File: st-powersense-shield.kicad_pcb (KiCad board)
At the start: 2 copper layers, 7 parts, among them P1 Left_Header, P2 IDD, P3 Right_Header, U1 MAX4378

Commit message: Generated and added manufacturing data. Also added logos to repository.
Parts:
- added G***: UoB_Logo, UoB_Logo-sm-15, F.Cu at (131.8, 108.0)
- added G***: LOGO, LOGO-mageec-smaller, F.Cu at (108.9, 103.8)
- added P4: MEAS_2, SIL-3, F.Cu at (117.9, 88.4)
- added P5: AMP_4, SIL-2, F.Cu at (134.0, 87.5)
- added P6: MEAS_4, SIL-3, F.Cu at (135.3, 93.2)
- added P7: MEAS_3, SIL-3, F.Cu at (135.3, 101.5)
- P1: value Left_Header -> Left_Discovery_Header
- P3: value Right_Header -> Right_Discovery_Header
- moved C2 43.4 mm to (125.7, 85.9), turned to 180 degrees
- moved C1 36.7 mm to (125.9, 89.0), turned to 180 degrees
- moved U1 30.5 mm to (126.2, 96.7), turned to 270 degrees
- moved R1 23.4 mm to (115.8, 99.5), turned to 270 degrees
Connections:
- P1 pad 13: /PA3 -> /ADC1
- U1 pad 1: /ADC1 -> /ADC2
- U1 pad 2: /IDD- -> N-000002
- U1 pad 3: /IDD+ -> N-000001
- U1 pad 5: N-0000042 -> /IDD+
- U1 pad 6: N-0000043 -> /IDD-
- U1 pad 7: N-0000044 -> /ADC1
- U1 pad 8: N-0000039 -> /ADC3
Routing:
- net GND: track 0.00 -> 101.3 mm, vias 0 -> 11
- net /ADC2: track 0.00 -> 61.0 mm
- net VAA: track 0.00 -> 40.6 mm
- net /ADC3: track 0.00 -> 34.1 mm
- net /ADC1: track 0.00 -> 28.1 mm
- net /IDD-: track 0.00 -> 21.7 mm
- net /IDD+: track 0.00 -> 16.5 mm
- net N-000002: track 0.00 -> 8.53 mm
- net N-000001: track 0.00 -> 7.80 mm
- net N-0000027: track 0.00 -> 7.57 mm
- net N-000004: track 0.00 -> 7.00 mm
- net N-000003: track 0.00 -> 6.47 mm
- net N-0000026: track 0.00 -> 6.40 mm
- net N-0000025: track 0.00 -> 6.18 mm
- added copper zone on B.Cu, net GND
- added copper zone on F.Cu, net GND
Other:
- board outline added: 60 x 30 mm
- net class Default: clearance 0.254 -> 0.2; trace_width 0.254 -> 0.3; via_dia 0.889 -> 0.5; via_drill 0.635 -> 0.3
- rule trace_clearance: 0.254 -> 0.2
- rule trace_min: 0.254 -> 0.15
- rule via_min_drill: 0.508 -> 0.2
- rule via_min_size: 0.889 -> 0.3
- board text added: "Back Copper"
- board text added: "Back Silkscreen"
- board text added: "Back Solder Mask"
- board text added: "Build information ========== 2 Layer 1oz FO4 60x30mm 11 Vias Silkscreen Front only ** Through-hole sockets mounted on rear ** Queries: contact simon@cs.bris.ac.uk"
- board text added: "Designer: Simon Hollis"
- board text added: "Ext #4 Out"
- board text added: "Front Copper"
- board text added: "Front Silkscreen"
- board text added: "Front Solder Mask"
- board text added: "Front Solder Paste"
- board text added: "IDD"
- board text added: "IDD Shunt"
- board text added: "MAGEEC & EACOP Projects"
- board text added: "Measure Ext #2"
- board text added: "Measure Ext #3"
- board text added: "Measure Ext #4"
- board text added: "ST Discovery STM32F407VG Power Measurement Shield"

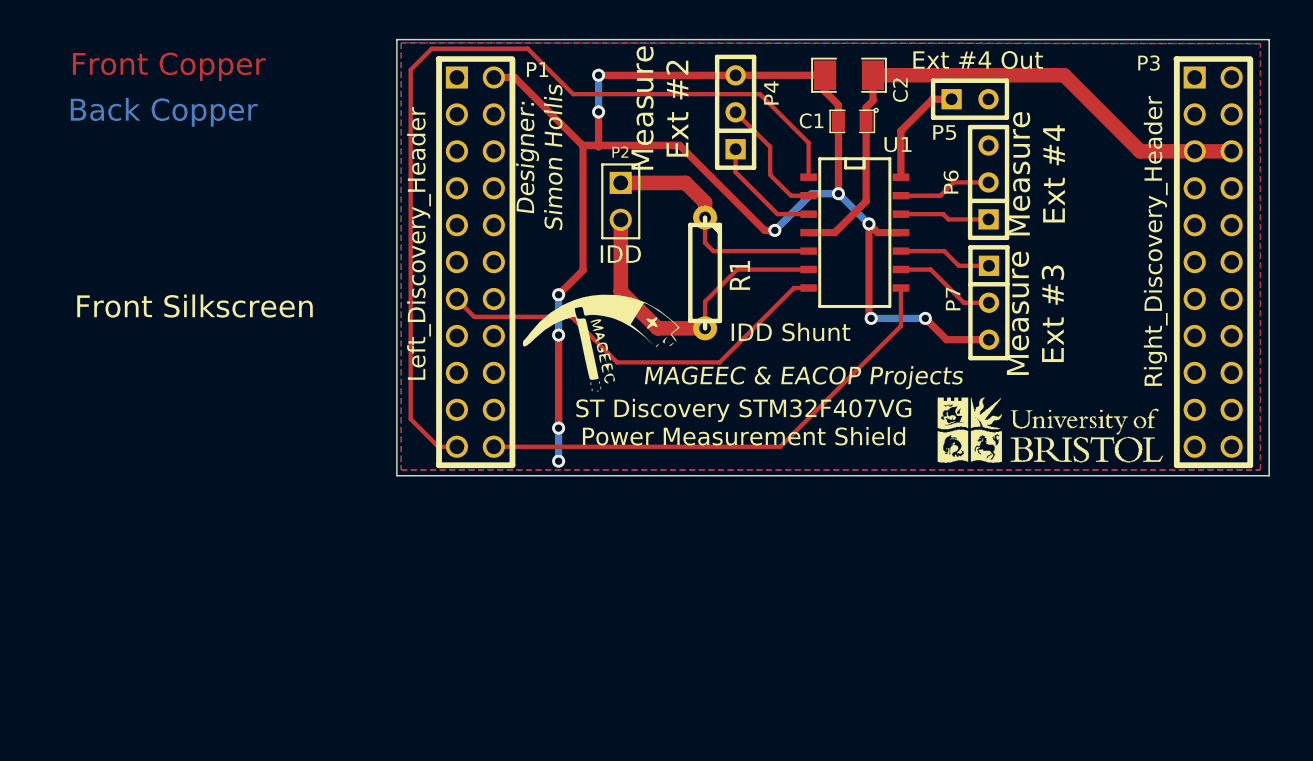
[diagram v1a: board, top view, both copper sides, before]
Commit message: Add v3 design and v2 and v3 manufacturing data.
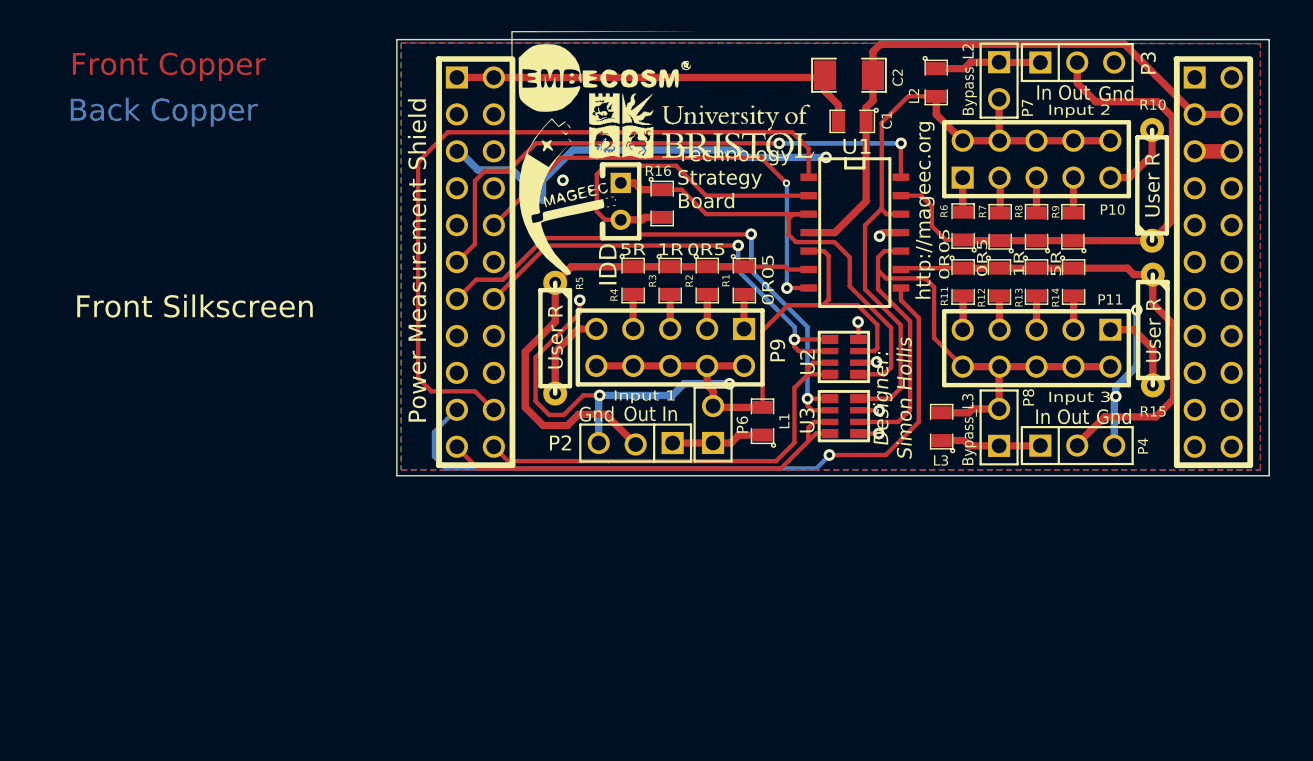
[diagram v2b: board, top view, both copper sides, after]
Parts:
- added G***: LOGO, LOGO-embecosm-150px, F.Cu at (108.8, 85.8)
- added L1: 2.2uH, SM0805, F.Cu at (119.8, 109.7)
- added L2: 2.2uH, SM0805, F.Cu at (131.7, 86.4)
- added L3: 2.2uH, SM0805, F.Cu at (132.1, 110.0)
- added P10: R_select_2, PIN_ARRAY_5x2, F.Cu at (138.6, 91.7)
- added P11: R_select_3, PIN_ARRAY_5x2, F.Cu at (138.6, 104.7)
- added P3: Input_2, PIN_ARRAY_3X1, F.Cu at (141.4, 85.0)
- added P8: Bypass_L3, PIN_ARRAY_2X1, F.Cu at (136.0, 110.1)
- added P9: R_select_1, PIN_ARRAY_5x2, F.Cu at (113.4, 104.6)
- added R10: UserR, R3-LARGE_PADS, F.Cu at (146.6, 93.5)
- added R11: 0R05, SM0805, F.Cu at (133.6, 100.1)
- added R12: 0R5, SM0805, F.Cu at (136.1, 100.1)
- added R13: 1R, SM0805, F.Cu at (138.6, 100.1)
- added R14: 5R, SM0805, F.Cu at (141.2, 100.1)
- added R15: UserR, R3-LARGE_PADS, F.Cu at (146.6, 103.4)
- added R16: 0R5, SM0805, F.Cu at (112.8, 94.7)
- added R2: 0R5, SM0805, F.Cu at (116.0, 100.0)
- added R3: 1R, SM0805, F.Cu at (113.4, 100.0)
- added R4: 5R, SM0805, F.Cu at (110.8, 100.0)
- added R5: UserR, R3-LARGE_PADS, F.Cu at (105.5, 104.0)
- added R6: 0R05, SM0805, F.Cu at (133.6, 96.2)
- added R7: 0R5, SM0805, F.Cu at (136.1, 96.3)
- added R8: 1R, SM0805, F.Cu at (138.6, 96.3)
- added R9: 5R, SM0805, F.Cu at (141.1, 96.3)
- added U2: 1k, ACAS-0612, F.Cu at (125.3, 105.2)
- added U3: 1k, ACAS-0612, F.Cu at (125.3, 109.3)
- P1: value Left_Discovery_Header -> Left_Header
- P12: renamed from P3; value Right_Discovery_Header -> Right_Header
- P2: value IDD -> Input_1; footprint PIN_ARRAY_2X1 -> PIN_ARRAY_3X1
- P4: value MEAS_2 -> Input_3; footprint SIL-3 -> PIN_ARRAY_3X1
- P5: value AMP_4 -> IDD
- P6: value MEAS_4 -> Bypass_L1; footprint SIL-3 -> PIN_ARRAY_2X1
- P7: value MEAS_3 -> Bypass_L2; footprint SIL-3 -> PIN_ARRAY_2X1
- R1: value R -> 0R05; footprint R3-LARGE_PADS -> SM0805
- moved P4 32.8 mm to (141.4, 111.3), turned to 0 degrees
- moved G*** 31.8 mm to (107.8, 87.1)
- moved P6 25.2 mm to (116.3, 109.9)
- moved P5 25.0 mm to (110.0, 94.5), turned to 270 degrees
- moved P2 16.7 mm to (111.0, 111.2), turned to 180 degrees
- moved P7 15.3 mm to (136.0, 86.2)
- moved G*** 10.3 mm to (105.9, 94.0), turned to 90 degrees
- moved R1 2.75 mm to (118.5, 100.0)
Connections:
- P1 pad 10: /PC2 -> /Amp_1
- P1 pad 11: /PA1 -> /Amp_2
- P1 pad 13: /ADC1 -> /PA3
- P1 pad 19: /PC5 -> /Amp_3
- P1 pad 20: /PC4 -> /Amp_uP
- P1 pad 21: /ADC2 -> /PB1
- P1 pad 22: /ADC3 -> /PB0
- P1 pad 6: N-0000029 (its old number) -> /NRST
- P12 pad 3: /5V -> VAA
- P12 pad 4: /5V -> VAA
- P12 pad 5: VAA -> /3V
- P12 pad 6: VAA -> /3V
- P2 pad 1: /IDD+ -> /In_1
- P2 pad 2: /IDD- -> /Out_1
- P4 pad 1: N-000001 -> /In_3
- P4 pad 2: N-000002 -> /Out_3
- P5 pad 1: N-0000027 (its old number) -> /uP_IDD+
- P5 pad 2: GND -> /uP_IDD-
- P6 pad 1: N-0000025 (its old number) -> /In_1
- P6 pad 2: N-0000026 (its old number) -> /R_In_1
- P7 pad 1: N-000003 -> /In_2
- P7 pad 2: N-000004 -> /R_In_2
- R1 pad 1: /IDD+ -> /Out_1
- R1 pad 2: /IDD- -> N-0000014
- U1 pad 1: /ADC2 -> /Amp_uP
- U1 pad 10: N-000003 -> /R_In_3
- U1 pad 12: N-0000025 (its old number) -> /R_In_2
- U1 pad 13: N-0000026 (its old number) -> /Out_2
- U1 pad 14: N-0000027 (its old number) -> /Amp_2
- U1 pad 2: N-000002 -> /uP_IDD-
- U1 pad 3: N-000001 -> /uP_IDD+
- U1 pad 5: /IDD+ -> /R_In_1
- U1 pad 6: /IDD- -> /Out_1
- U1 pad 7: /ADC1 -> /Amp_1
- U1 pad 8: /ADC3 -> /Amp_3
- U1 pad 9: N-000004 -> /Out_3
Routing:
- net /ADC2: track 61.0 -> 0.00 mm
- net /Amp_uP: track 0.00 -> 51.1 mm
- net /Amp_3: track 0.00 -> 48.6 mm, vias 0 -> 1
- net /R_In_2: track 0.00 -> 45.8 mm
- net /R_In_3: track 0.00 -> 44.9 mm
- net /R_In_1: track 0.00 -> 39.2 mm
- net /Amp_2: track 0.00 -> 38.9 mm, vias 0 -> 2
- net /PA3: track 0.00 -> 38.7 mm, vias 0 -> 2
- net /Out_2: track 0.00 -> 37.4 mm
- net /Out_1: track 0.00 -> 36.7 mm
- net /Out_3: track 0.00 -> 34.8 mm
- net /ADC3: track 34.1 -> 0.00 mm
- net /uP_IDD+: track 0.00 -> 32.4 mm
- net /PA2: track 0.00 -> 31.9 mm, vias 0 -> 2
- net /Amp_1: track 0.00 -> 31.5 mm, vias 0 -> 2
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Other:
- rule pad_to_mask_clearance: 0 -> 0.08
- board text added: "0R05 0R5 1R 5R User"
- board text added: "Current measurements arescaled by +50x and voltages are scaled by +0.5x"
- board text added: "Discovery Board Connections ------------------ Input 1 Current: PC2 Input 1 Voltage: PA2 Input 2 Current: PA1 Input 2 Voltage: PA3 Input 3 Current: PC5 Input 3 Voltage: PB1 STM32F Current: PC4 STM32F Voltage: PB0"
- board text added: "For ST Discovery STM32F407VG"
- board text added: "Gnd"
- board text added: "In Out"
- board text added: "Input 1"
- board text added: "Input 2"
- board text added: "Input 3"
- board text added: "Jumper the "Bypass" connectors unless you have removed an inductor from DUT."
- board text added: "Out In"
- board text added: "P1"
- board text added: "P12"
- board text added: "P5"
- board text added: "Power Measurement Shield"
- board text added: "Technology Strategy Board"
- board text added: "User 5R 1R 0R5 0R05"
- board text added: "User R"
- board text added: "http://mageec.org"
- board text removed: "Ext #4 Out"
- board text removed: "IDD Shunt"
- board text removed: "MAGEEC & EACOP Projects"
- board text removed: "Measure Ext #2"
- board text removed: "Measure Ext #3"
- board text removed: "Measure Ext #4"
- board text removed: "ST Discovery STM32F407VG Power Measurement Shield"
